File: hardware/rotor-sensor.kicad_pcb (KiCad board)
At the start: 2 copper layers, 30.7 x 16 mm, 41 parts, among them J1 Conn_01x03, J2 Conn_01x03, J3 Conn_01x03, U1 ATtiny202-SS, U2 EE-SX199, U3 SM351LT

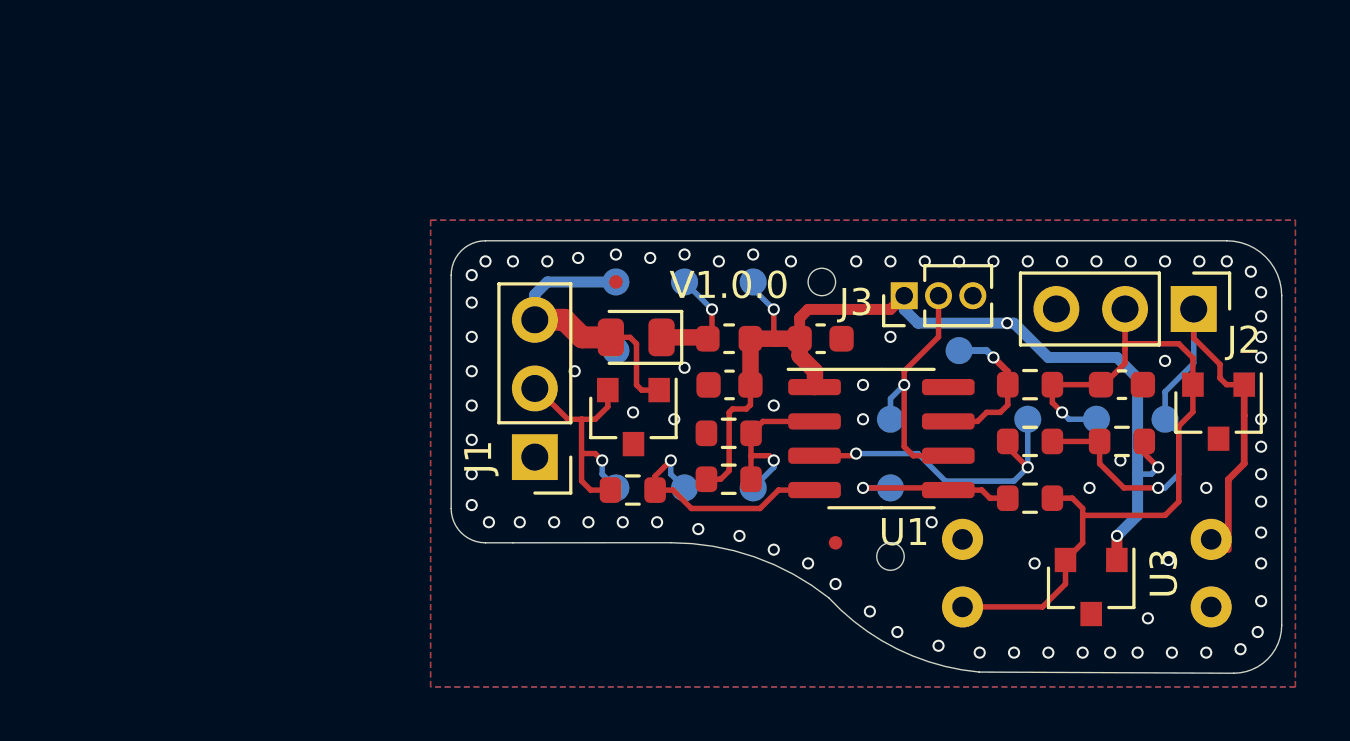
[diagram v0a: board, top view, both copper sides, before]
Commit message: Adds LIN Transceiver to the design
Updates layout and schematic
Adds overcurrent protection IC and removes sense line
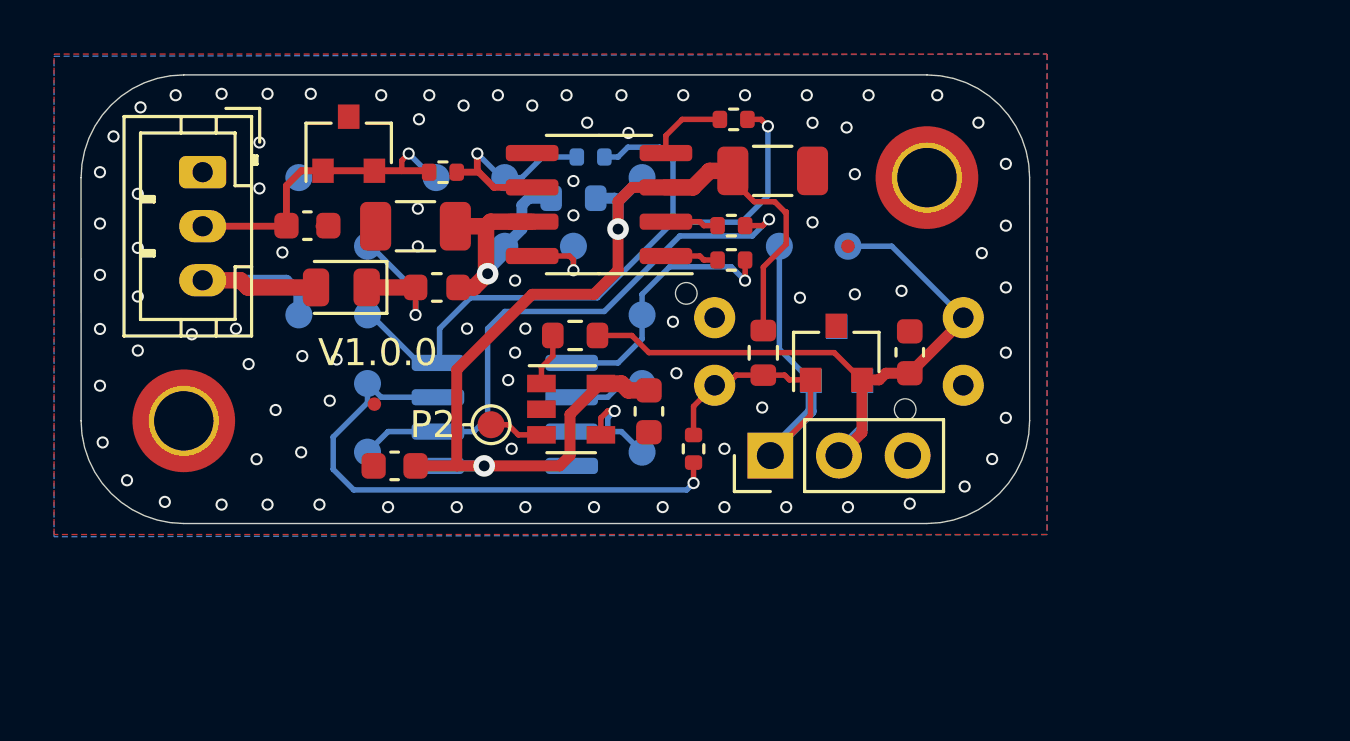
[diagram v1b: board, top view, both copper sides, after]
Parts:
- removed J3: Conn_01x03, Connector_PinHeader_1.27mm:PinHeader_1x03_P1.27mm_Vertical
- removed the R5 at (3.23, -1.80)
- removed the R6 at (-7.92, -0.40)
- removed REF** (x6): Tab, local:Tab
- added C2: 10u, Capacitor_SMD:C_1206_3216Metric, F.Cu at (-6.30, -11.8)
- added C3: 22p, Capacitor_SMD:C_0603_1608Metric, F.Cu at (-23.5, -9.78)
- added C5: 100n, Capacitor_SMD:C_0603_1608Metric, F.Cu at (-10.9, -2.91)
- added H1: MountingHole_Pad, MountingHole:MountingHole_2.2mm_M2_DIN965_Pad_TopOnly, F.Cu at (-28.1, -2.56)
- added H2: MountingHole_Pad, MountingHole:MountingHole_2.2mm_M2_DIN965_Pad_TopOnly, F.Cu at (-0.59, -11.6)
- added R1: 0, Resistor_SMD:R_0402_1005Metric, B.Cu at (-13.0, -12.3)
- added R2: 0, Resistor_SMD:R_0402_1005Metric, F.Cu at (-7.83, -8.51)
- added R3: 0, Resistor_SMD:R_0402_1005Metric, F.Cu at (-7.74, -13.7)
- added R9: 0, Resistor_SMD:R_0603_1608Metric, B.Cu at (-13.7, -10.8)
- added TP17: P2, TestPoint:TestPoint_Pad_D1.0mm, F.Cu at (-16.7, -2.42)
- added TP4: V3, TestPoint:TestPoint_Pad_D1.0mm, B.Cu at (-11.1, -11.6)
- added TP7: C1, TestPoint:TestPoint_Pad_D1.0mm, B.Cu at (-16.2, -11.6)
- added TP8: C2, TestPoint:TestPoint_Pad_D1.0mm, B.Cu at (-13.7, -9.02)
- added U2: MCP2021A-xxxxSN, Package_SO:SOIC-8_3.9x4.9mm_P1.27mm, F.Cu at (-12.7, -10.6)
- added U5: AP22804AW5, Package_TO_SOT_SMD:SOT-23-5, F.Cu at (-13.8, -2.99)
- C1: value 100n -> 10u; footprint Capacitor_SMD:C_0603_1608Metric -> Capacitor_SMD:C_1206_3216Metric
- J1: footprint Connector_PinHeader_2.54mm:PinHeader_1x03_P2.54mm_Vertical -> Connector_JST:JST_PH_B3B-PH-K_1x03_P2.00mm_Vertical
- R4: value 50m -> 0; footprint Resistor_SMD:R_0603_1608Metric -> Resistor_SMD:R_0402_1005Metric
- R5: renamed from R1; value 50m -> 0; footprint Resistor_SMD:R_0603_1608Metric -> Resistor_SMD:R_0402_1005Metric
- R7: value 1k -> 0; footprint Resistor_SMD:R_0603_1608Metric -> Resistor_SMD:R_0402_1005Metric
- TP1: value + -> V0
- TP10: renamed from TP7; value COMB -> M1
- TP11: renamed from TP8; value W2 -> M2
- TP12: renamed from TP9; value SENSE -> M3
- TP13: renamed from TP10; value AC- -> M6
- TP14: renamed from TP12; value IN -> P0
- TP15: renamed from TP11; value AC+ -> M7
- TP16: renamed from TP13; value OUT -> P1
- TP2: value COMA -> V1
- TP3: renamed from TP4; value VCC -> V2
- TP5: value - -> V4
- TP6: renamed from TP3; value VD -> C0
- TP9: renamed from TP6; value UPDI -> M0
- U3: moved to B.Cu
- U4: renamed from U1; moved to B.Cu
- moved TP15 24.5 mm to (-21.3, -3.94)
- moved R8 17.9 mm to (-13.6, -5.72)
- moved FID2 17.8 mm to (-21.0, -3.18)
- moved J2 16.6 mm to (-6.39, -1.27), turned to 90 degrees
- moved C4 16.5 mm to (-20.3, -0.89), turned to 180 degrees
- moved J1 16.2 mm to (-27.4, -11.8), turned to 270 degrees
- moved TP14 15.6 mm to (-6.05, -9.02)
- moved D2 14.6 mm to (-22.0, -12.8), turned to 90 degrees
- moved TP13 14.3 mm to (-21.3, -1.40)
- moved D3 14.3 mm to (-3.95, -5.08), turned to 90 degrees
- moved U4 14.0 mm to (-16.2, -2.80)
- moved R5 13.7 mm to (-18.5, -11.8)
- moved R6 13.7 mm to (-6.65, -5.08), turned to 90 degrees
- moved TP10 13.4 mm to (-21.3, -6.48)
- moved TP5 13.4 mm to (-23.8, -11.6)
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- renumbered C2 to C4, C3 to C6, D2 to D1, D1 to D2, FID2 to FID1, FID1 to FID2, R2 to R6, R3 to R8, U2 to U1
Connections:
- C1 pad 1: +5V -> /VIN_FILT
- D1 pad 1: Net-(D2-Pad1) -> Net-(D1-Pad1)
- D1 pad 2: /Vin -> /VIN
- D2 pad 1: /Vin -> /LIN_IN
- D2 pad 2: Net-(D1-Pad2) -> /LIN_IN
- J1 pad 2: Net-(D1-Pad2) -> /LIN_IN
- J1 pad 3: /Vin -> /VIN
- L1 pad 1: Net-(D2-Pad1) -> Net-(D1-Pad1)
- L1 pad 2: +5V -> /VIN_FILT
- R4 pad 1: PA3_ADC0_AIN3 -> PA6_GPIO
- R4 pad 2: /OS_OUTPUT -> Net-(R4-Pad2)
- R5 pad 1: PA1_USART0_TXD -> /LIN_BUS
- R5 pad 2: Net-(D1-Pad2) -> /LIN_IN
- R7 pad 1: PA6_AC0_AINN0 -> /OS_INPUT
- R7 pad 2: GND -> PA7_AC0_AINP0
- R8 pad 1: PA2_TCA2_W2 -> Net-(R8-Pad1)
- TP1 pad 1: /Vin -> /VIN
- TP11 pad 1: PA2_TCA2_W2 -> PA2_USART0_RXD
- TP12 pad 1: PA3_ADC0_AIN3 -> PA3_TCA0_W0
- TP13 pad 1: PA6_AC0_AINN0 -> PA6_GPIO
- TP2 pad 1: Net-(D1-Pad2) -> Net-(D1-Pad1)
- TP3 pad 1: +5V -> /VIN_FILT
- TP6 pad 1: Net-(D2-Pad1) -> /LIN_IN
- U3 pad 1: +5V -> /OS_OUTPUT
- U3 pad 2: /OS_OUTPUT -> /OS_INPUT
- U4 pad 2: PA6_AC0_AINN0 -> PA6_GPIO
- U4 pad 5: PA2_TCA2_W2 -> PA2_USART0_RXD
- U4 pad 7: PA3_ADC0_AIN3 -> PA3_TCA0_W0
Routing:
- net PA6_GPIO: track 0.00 -> 21.3 mm, vias 0 -> 1
- net PA1_USART0_TXD: track 9.03 -> 27.4 mm
- net /LIN_IN: track 0.00 -> 12.2 mm, vias 0 -> 1
- net /Vin: track 10.8 -> 0.00 mm
- net /VIN_FILT: track 0.00 -> 10.2 mm, vias 0 -> 1
- net PA2_USART0_RXD: track 0.00 -> 9.83 mm, vias 0 -> 1
- net Net-(D1-Pad2): track 9.57 -> 0.00 mm, vias 1 -> 0
- net PA7_AC0_AINP0: track 11.6 -> 21.0 mm, vias 2 -> 1
- net /VIN: track 0.00 -> 8.87 mm
- net /LIN_BUS: track 0.00 -> 8.10 mm, vias 0 -> 1
- net PA0_UPDI: track 9.36 -> 2.82 mm, vias 1 -> 0
- net PA2_TCA2_W2: track 6.53 -> 0.00 mm, vias 1 -> 0
- net PA6_AC0_AINN0: track 6.48 -> 0.00 mm, vias 1 -> 0
- net Net-(D1-Pad1): track 0.00 -> 6.17 mm, vias 0 -> 1
- net PA3_ADC0_AIN3: track 5.80 -> 0.00 mm, vias 1 -> 0
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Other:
- board size 30.7 x 16 mm -> 35.1 x 16.6 mm

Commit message: Panelize?
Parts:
- added D4: LED_Small, LED_SMD:LED_0603_1608Metric, F.Cu at (-20.9, -4.45)
- added R10: 220, Resistor_SMD:R_0603_1608Metric, F.Cu at (-17.6, -4.45)
- moved FID2 3.28 mm to (-24.3, -3.81)
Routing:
- net Net-(R10-Pad2): track 1.95 -> 4.07 mm
- net Net-(D4-Pad2): track 0.00 -> 1.65 mm
- net GND: vias 87 -> 82
